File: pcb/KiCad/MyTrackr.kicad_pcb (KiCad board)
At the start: 2 copper layers, 50 x 50 mm, 40 parts, among them CN1 GPS_ANTENNA, CON1 MICRO_SD, J1 REGULATOR_3V3, J2 CONN_ICSP, J3 CONN_SERIAL, J4 CONN_BAT, P1 CONN_OLED, Q1 Q_PMOS_GSD, SW1 BTN_RESET, SW2 BTN_SEL, SW3 BTN_NEXT, SW4 BTN_PREV, SW5 BTN_BACK, U1 ATMEGA328PA, U2 GPS-NEO-6M, U3 24AA32

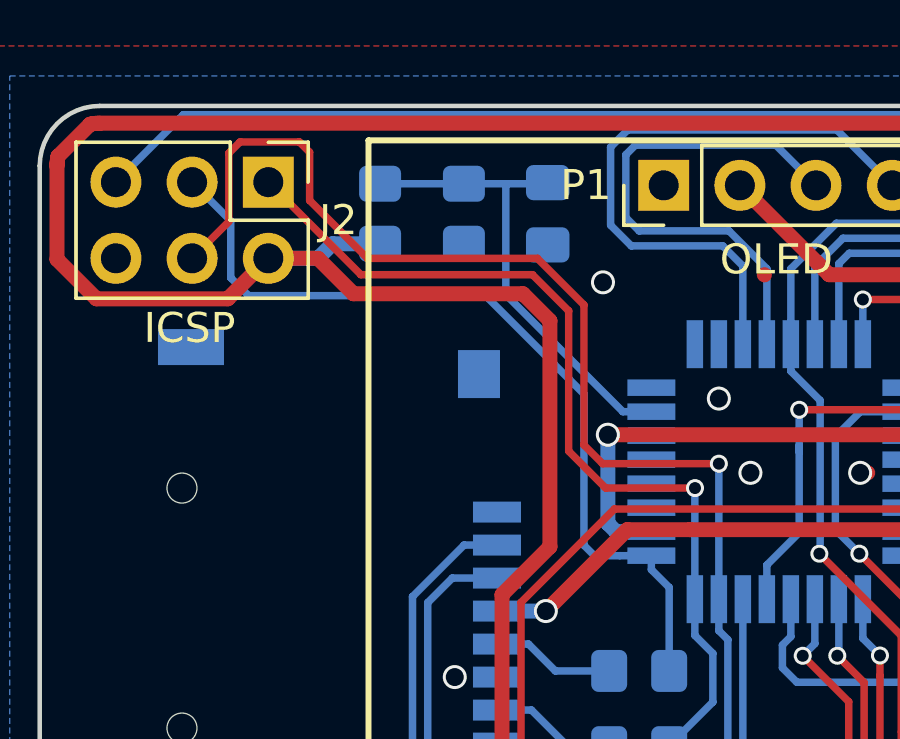
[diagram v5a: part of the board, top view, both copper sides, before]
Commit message: Connect all grounds, use meaningful signal names
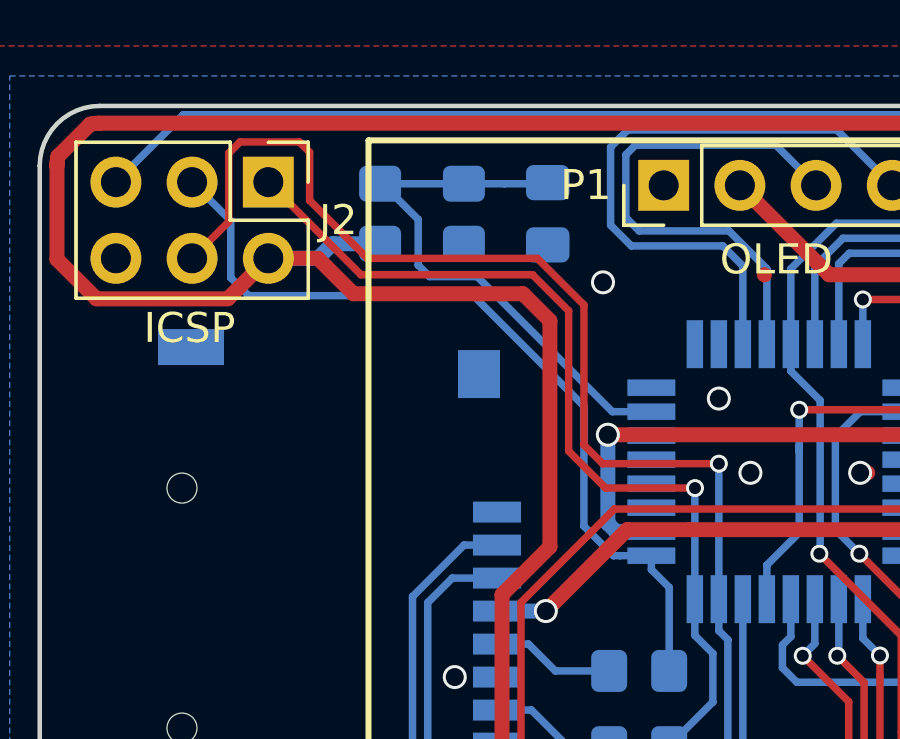
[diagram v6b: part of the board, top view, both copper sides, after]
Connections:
- net /ARDUINO_PIN_4 renamed /sel
- net /ARDUINO_PIN_5 renamed /next
- net /ARDUINO_PIN_6 renamed /prev
- net /ARDUINO_PIN_7 renamed /back
- net /ARDUINO_PIN_8 renamed /~peripherals_power
- net /ARDUINO_PIN_9 renamed /act_led
- U1 pad 21: (no net) -> GND
- U1 pad 5: (no net) -> GND
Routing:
- net Net-(C5-Pad1): track 15.9 -> 18.8 mm
- net /SCK: track 28.6 -> 28.0 mm

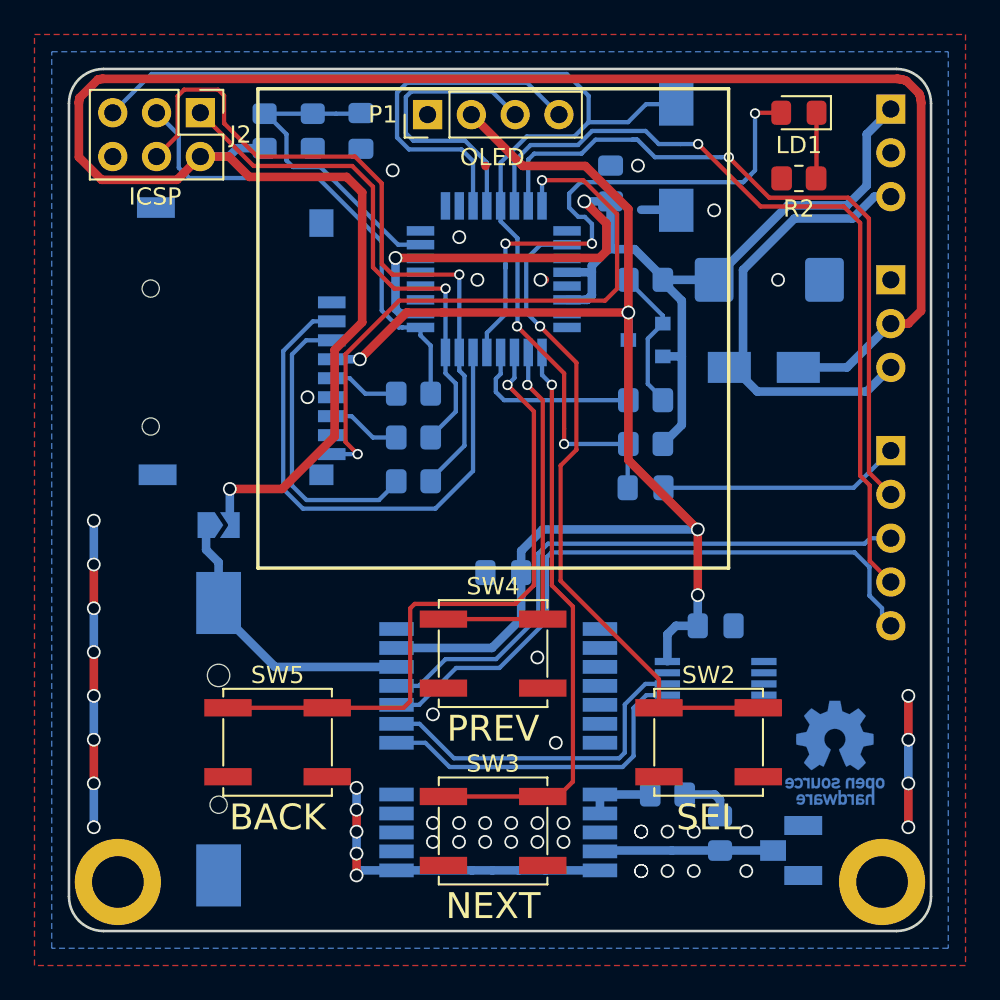
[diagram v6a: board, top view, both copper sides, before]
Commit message: Use KiCad's 328 symbol and add MOSFET-bypass jumper
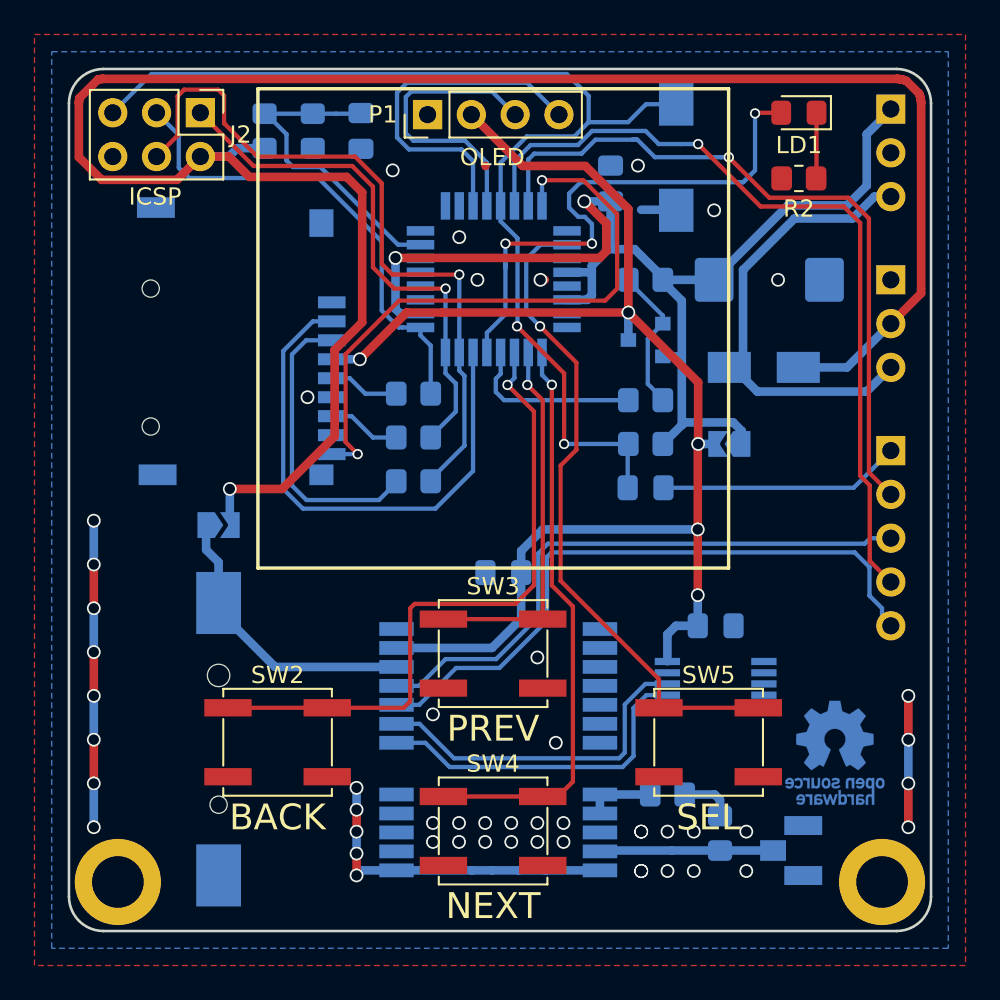
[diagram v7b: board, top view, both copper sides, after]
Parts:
- added JP2: JMP_PERIP, Jumper:SolderJumper-2_P1.3mm_Open_TrianglePad1.0x1.5mm, B.Cu at (128.3, 71.8)
- U1: value ATMEGA328PA -> ATmega328P-AU
- turned C3 to 0 degrees
- renumbered SW5 to SW2, SW4 to SW3, SW3 to SW4, SW2 to SW5
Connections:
- net /328_RX renamed /rx_328
- net /328_TX renamed /tx_328
- net /DTR renamed /~dtr
- net /GPS_RX renamed /rx_gps
- net /GPS_TX renamed /tx_gps
- net /MISO renamed /miso
- net /MOSI renamed /mosi
- net /RESET renamed /~reset
- net /SCK renamed /sck
- net /VBAT renamed VBAT
- net /VCHG renamed +5V
- net /~peripherals_power renamed /~peripherals
- net Net-(P1-Pad3) renamed /scl
- net Net-(P1-Pad4) renamed /sda
- C3 pad 1: VPP -> GND
- C3 pad 2: GND -> VPP
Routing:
- net +3V3: track 65.6 -> 70.1 mm
- net VPP: track 83.5 -> 84.6 mm, vias 4 -> 5
- net VBAT: track 120.0 -> 119.4 mm

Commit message: Make custom footprint for reset button
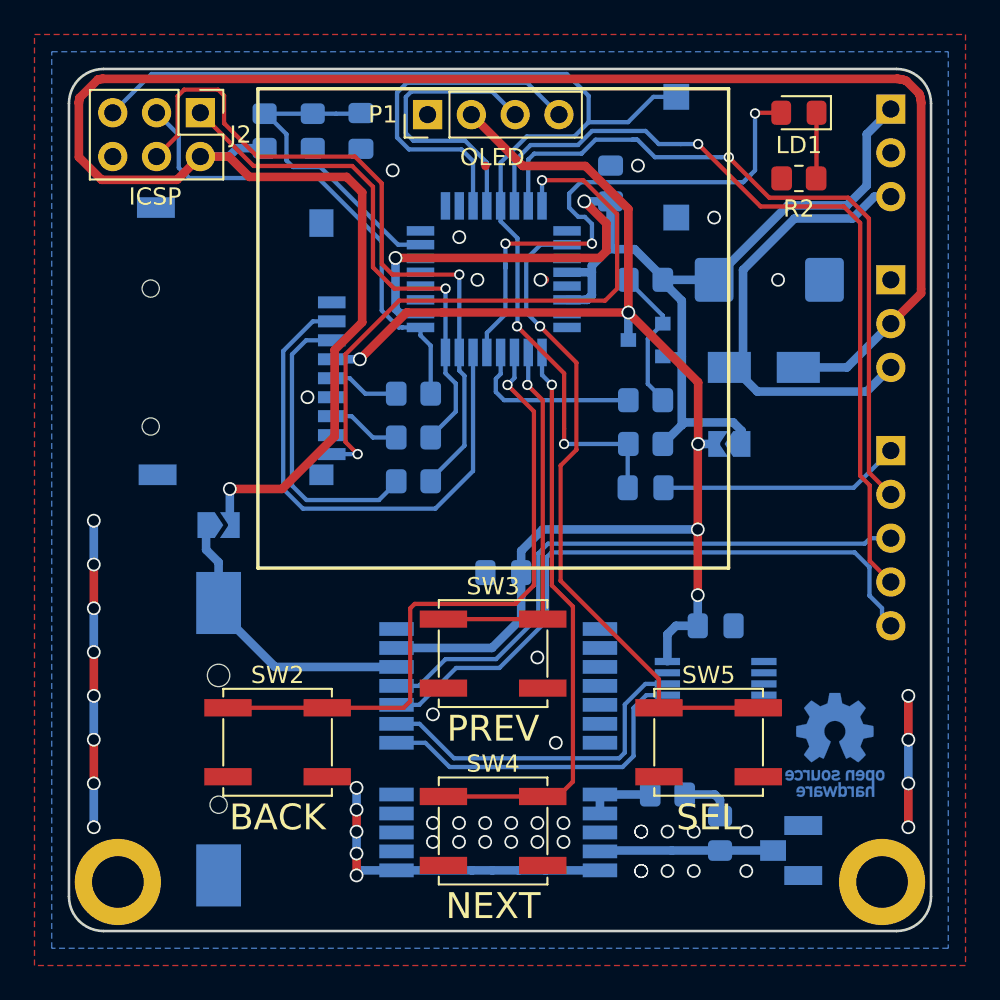
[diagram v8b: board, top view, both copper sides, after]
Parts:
- SW1: footprint Button_Switch_SMD:SW_SPST_REED_CT05-XXXX-J1 -> MyTrackr:SingleButtonSmall
- moved V0 0.46 mm to (134.4, 89.2)
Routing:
- net GND: track 51.2 -> 49.2 mm
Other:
- board text added: "VIN"
- board text added: "VOUT"
- board text removed: "Vi"
- board text removed: "Vo"
